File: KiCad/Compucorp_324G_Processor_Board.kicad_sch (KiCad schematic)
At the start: 9 parts, among them J5 Processor Interboard, J6 Unused Connector, U5 TMC 1872, U6 TMC 1866, U7 TMC 1867, U8 TMC 1870

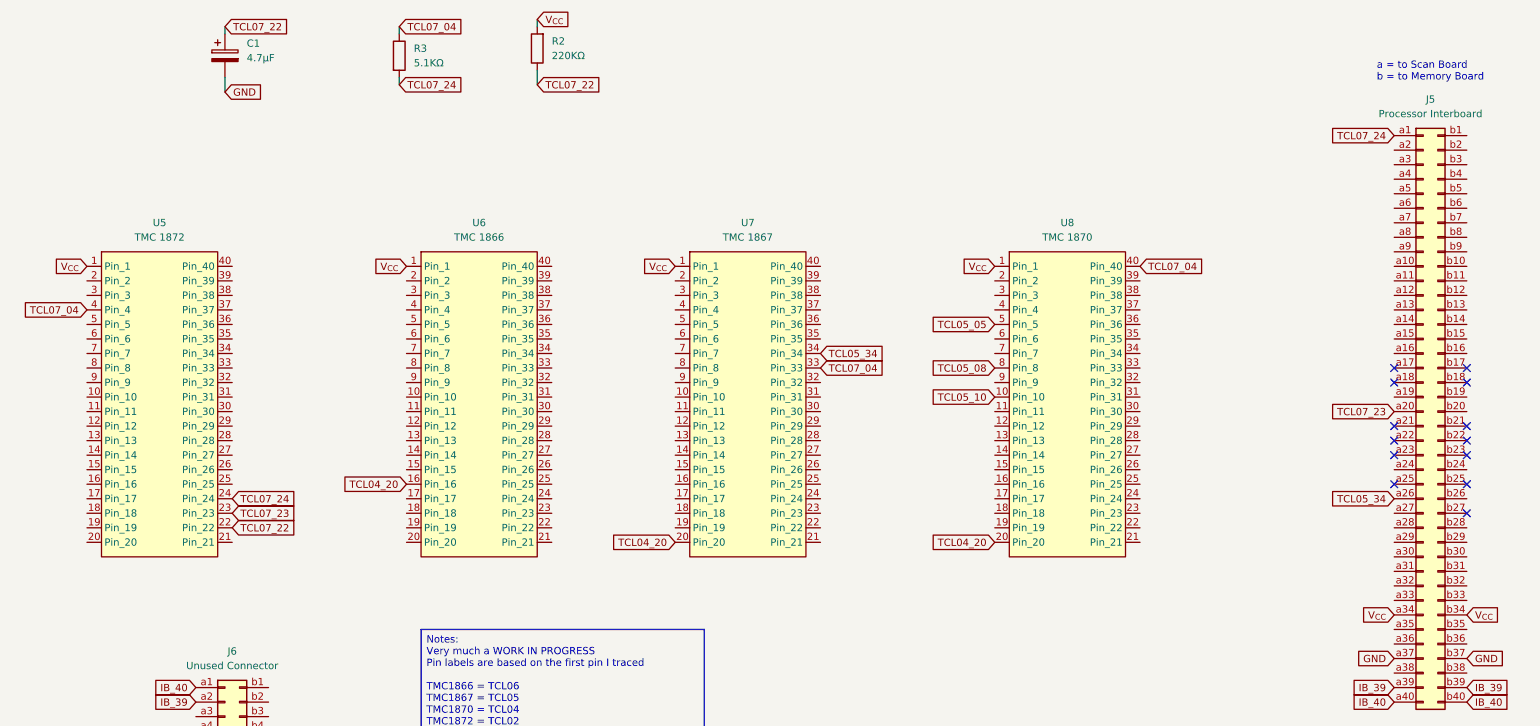
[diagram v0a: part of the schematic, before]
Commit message: Started on other board schematics
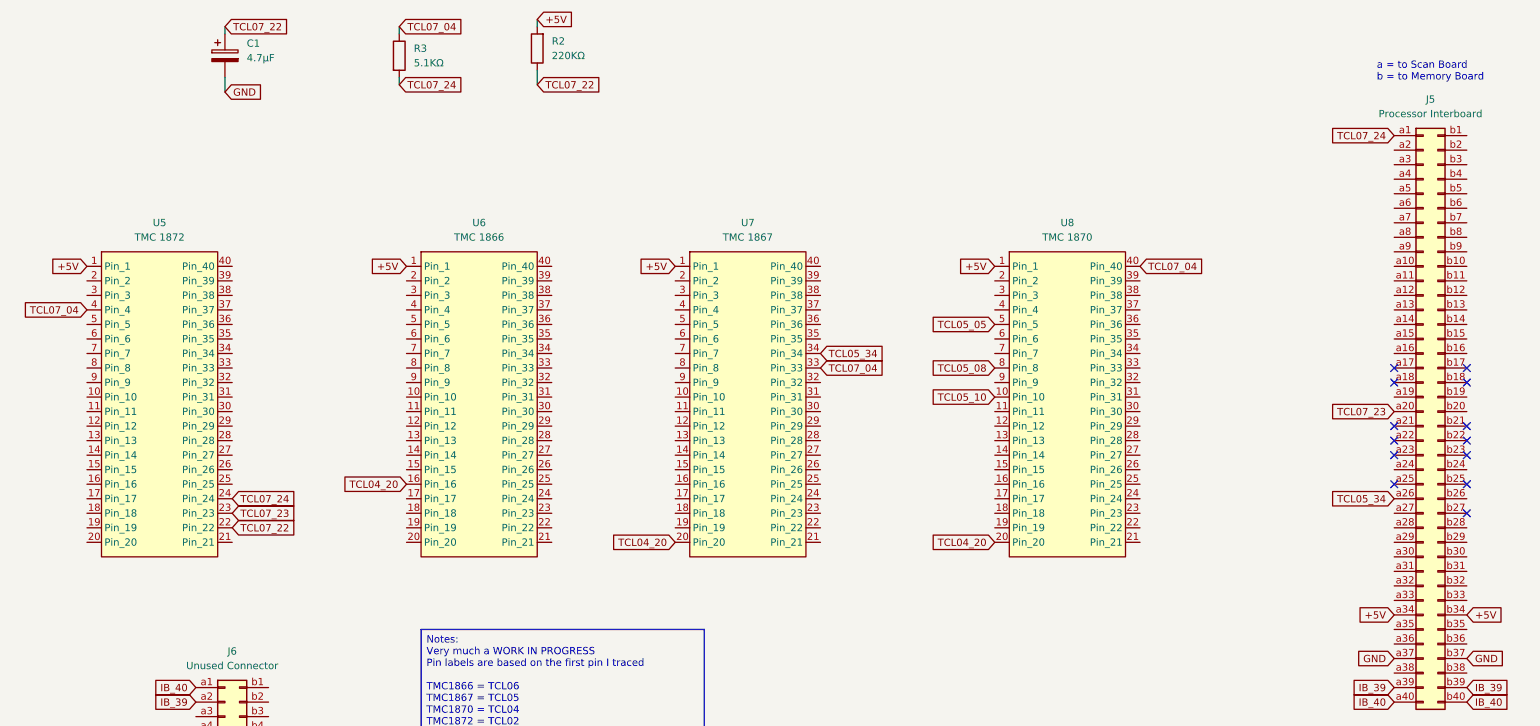
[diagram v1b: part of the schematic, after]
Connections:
- net V_{CC} renamed +5V
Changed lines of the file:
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@@
 		)
 	)
-	(global_label "V_{CC}"
+	(global_label "+5V"
 		(shape input)
 		(at 81.28 68.58 180)
@@
 		)
 	)
-	(global_label "V_{CC}"
+	(global_label "+5V"
 		(shape input)
 		(at 128.27 68.58 180)
@@
 		)
 	)
-	(global_label "V_{CC}"
+	(global_label "+5V"
 		(shape input)
 		(at 266.7 129.54 0)
@@
 		)
 	)
-	(global_label "V_{CC}"
+	(global_label "+5V"
 		(shape input)
 		(at 254 129.54 180)
@@
 		)
 	)
-	(global_label "V_{CC}"
+	(global_label "+5V"
 		(shape input)
 		(at 25.4 68.58 180)
@@
 		)
 	)
-	(global_label "V_{CC}"
+	(global_label "+5V"
 		(shape input)
 		(at 184.15 68.58 180)
@@
 		)
 	)
-	(global_label "V_{CC}"
+	(global_label "+5V"
 		(shape input)
 		(at 104.14 25.4 0)

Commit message: Started Memory Board schematic
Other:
- title: Compucorp 320-Series Processor Board -> Compucorp 300-Series Processor Board
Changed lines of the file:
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@@
 	(generator "eeschema")
 	(generator_version "9.0")
-	(paper "A4")
+	(paper "A3")
 	(title_block
-		(title "Compucorp 320-Series Processor Board")
+		(title "Compucorp 300-Series Processor Board")
 		(date "2/FEB/2026")
 		(rev "WIP")

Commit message: Memory board updates
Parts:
- removed U5: TMC 1872, symbol Compucorp_324G_Scientist:TMC_1872
- removed U6: TMC 1866, symbol Compucorp_324G_Scientist:TMC_1866
- removed U7: TMC 1867, symbol Compucorp_324G_Scientist:TMC_1867
- removed U8: TMC 1870, symbol Compucorp_324G_Scientist:TMC_1870
- added U5: TMC1872 (TCL07), symbol Compucorp_324G_Scientist:TMC1872
- added U6: TMC1866 (TCL06), symbol Compucorp_324G_Scientist:TMC1866
- added U7: TMC1867 (TCL05), symbol Compucorp_324G_Scientist:TMC1867
- added U8: TMC1870 (TCL04), symbol Compucorp_324G_Scientist:TMC1870
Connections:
- net +5V: now also U5.1 (Pin_1), U6.1 (Pin_1), U7.1 (Pin_1), U8.1 (Pin_1)
- net TCL04_20: now also U6.16 (Pin_16), U7.20 (Pin_20), U8.20 (Pin_20)
- net TCL05_05: now also U8.5 (Pin_5)
- net TCL05_08: now also U8.8 (Pin_8)
- net TCL05_10: now also U8.10 (Pin_10)
- net TCL05_34: now also U7.34 (Pin_34)
- net TCL07_04: now also U5.4 (Pin_4), U7.33 (Pin_33), U8.40 (Pin_40)
- net TCL07_22: now also U5.22 (Pin_22)
- net TCL07_23: now also U5.23 (Pin_23)
- net TCL07_24: now also U5.24 (Pin_24)
- net IB_10: now reaches J5.b10 (Pin_b10)
- net IB_02: now reaches J5.b2 (Pin_b2)
- net IB_28: now reaches J5.b28 (Pin_b28)
- net IB_29: now reaches J5.b29 (Pin_b29)
- net IB_30: now reaches J5.b30 (Pin_b30)
- net IB_31: now reaches J5.b31 (Pin_b31)
- net IB_33: now reaches J5.b33 (Pin_b33)
- net IB_09: now reaches J5.b9 (Pin_b9)

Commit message: Memory board updates
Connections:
- net IB_01: now reaches J5.b1 (Pin_b1)
- net IB_11: now reaches J5.b11 (Pin_b11)
- net TCL03_22: now reaches J5.b15 (Pin_b15)
- net IB_26: now reaches J5.b26 (Pin_b26)
- net IB_03: now reaches J5.b3 (Pin_b3)
- net IB_32: now reaches J5.b32 (Pin_b32)
- net IB_04: now reaches J5.b4 (Pin_b4)
- net IB_05: now reaches J5.b5 (Pin_b5)
- net IB_06: now reaches J5.b6 (Pin_b6)
- net IB_07: now reaches J5.b7 (Pin_b7)
- net IB_08: now reaches J5.b8 (Pin_b8)

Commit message: Update Compucorp_324G_Processor_Board.kicad_sch
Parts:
- J6: value Unused Connector -> Test Connector
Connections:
- net TCL03_22 is gone; now on net IB_15: J5.b15 (Pin_b15)
- net TCL07_23 is gone; now on net IB_20: J5.a20 (Pin_a20), U5.23 (Pin_23)
- net IB_01: now also J5.a1 (Pin_a1), R3.2, U5.24 (Pin_24), U7.33 (Pin_33), U8.40 (Pin_40)
- net IB_02: now also J5.a2 (Pin_a2), U6.27 (Pin_27), U7.15 (Pin_15), U8.15 (Pin_15)
- net IB_03: now also J5.a3 (Pin_a3), U5.2 (Pin_2), U6.25 (Pin_25), U7.14 (Pin_14), U8.16 (Pin_16)
- net IB_04: now also J5.a4 (Pin_a4), U5.40 (Pin_40), U6.24 (Pin_24), U7.13 (Pin_13), U8.17 (Pin_17)
- net IB_05: now also J5.a5 (Pin_a5), U5.39 (Pin_39), U6.23 (Pin_23), U7.12 (Pin_12), U7.18 (Pin_18), U8.18 (Pin_18)
- net IB_06: now also J5.a6 (Pin_a6), U5.38 (Pin_38), U6.22 (Pin_22), U7.11 (Pin_11), U8.19 (Pin_19)
- net IB_07: now also J5.a7 (Pin_a7), J6.a15 (Pin_a15), U5.10 (Pin_10), U6.18 (Pin_18), U8.23 (Pin_23)
- net IB_08: now also J5.a8 (Pin_a8), J6.a14 (Pin_a14), U5.9 (Pin_9), U6.17 (Pin_17), U8.24 (Pin_24)
- net IB_09: now also J5.a9 (Pin_a9), J6.a13 (Pin_a13), U6.20 (Pin_20), U8.25 (Pin_25)
- net IB_10: now also J5.a10 (Pin_a10), J6.a12 (Pin_a12), U6.19 (Pin_19), U8.26 (Pin_26)
- net IB_11: now also J5.a11 (Pin_a11), U5.21 (Pin_21), U8.21 (Pin_21)
- net IB_32: now also J5.a32 (Pin_a32), J6.a5 (Pin_a5), U5.34 (Pin_34), U6.40 (Pin_40), U7.8 (Pin_8), U8.38 (Pin_38)
- net IB_33: now also J5.a33 (Pin_a33), J6.a4 (Pin_a4)
- net TCL07_04: no longer U7.33 (Pin_33), U8.40 (Pin_40)
- net TCL07_22: now also J6.b14 (Pin_b14)
- net TCL07_24: no longer J5.a1 (Pin_a1), R3.2, U5.24 (Pin_24)
- net TCL04_22: now reaches U8.22 (Pin_22)
- net TCL04_22: now also U7.16 (Pin_16)
- net TCL07_37: now reaches J6.b13 (Pin_b13)
- net TCL07_37: now also U5.37 (Pin_37)
- net IB_38: now reaches J6.b15 (Pin_b15)
- net IB_38: now also J5.b38 (Pin_b38)
- net IB_15: now reaches U5.11 (Pin_11)
- net IB_15: now also J5.a15 (Pin_a15)
- net IB_12: now reaches J5.a12 (Pin_a12)
- net IB_12: now also J5.b12 (Pin_b12)
- net IB_13: now reaches J5.a13 (Pin_a13)
- net IB_13: now also J5.b13 (Pin_b13)
- net IB_14: now reaches J5.a14 (Pin_a14)
- net IB_14: now also J5.b14 (Pin_b14)
- net IB_20: now reaches J5.b20 (Pin_b20)
- no-connect marks 13 -> 20
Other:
- moved on the sheet: J5, U5, U6, U7, U8
